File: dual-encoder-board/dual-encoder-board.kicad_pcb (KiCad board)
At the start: 2 copper layers, 27.3 x 27.3 mm, 8 parts, among them U1 EC11EBB24C03

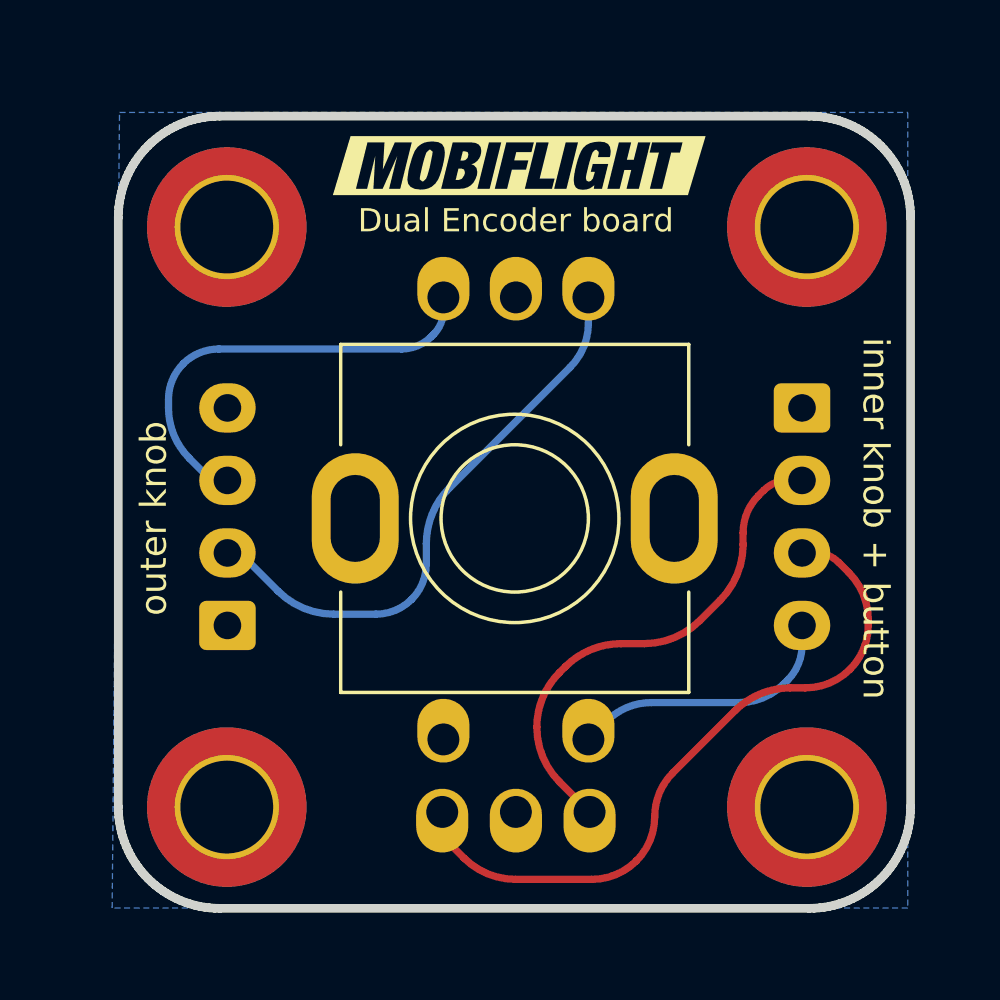
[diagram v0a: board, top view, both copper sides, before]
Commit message: Updates to pcb:   - centered the board outline to mounting holes, was slightly off   - moved the pin labels farther from JST's to avoid DRC errors   - change the unconnected pin 4 of outer knob to just "X" instead of "XX"
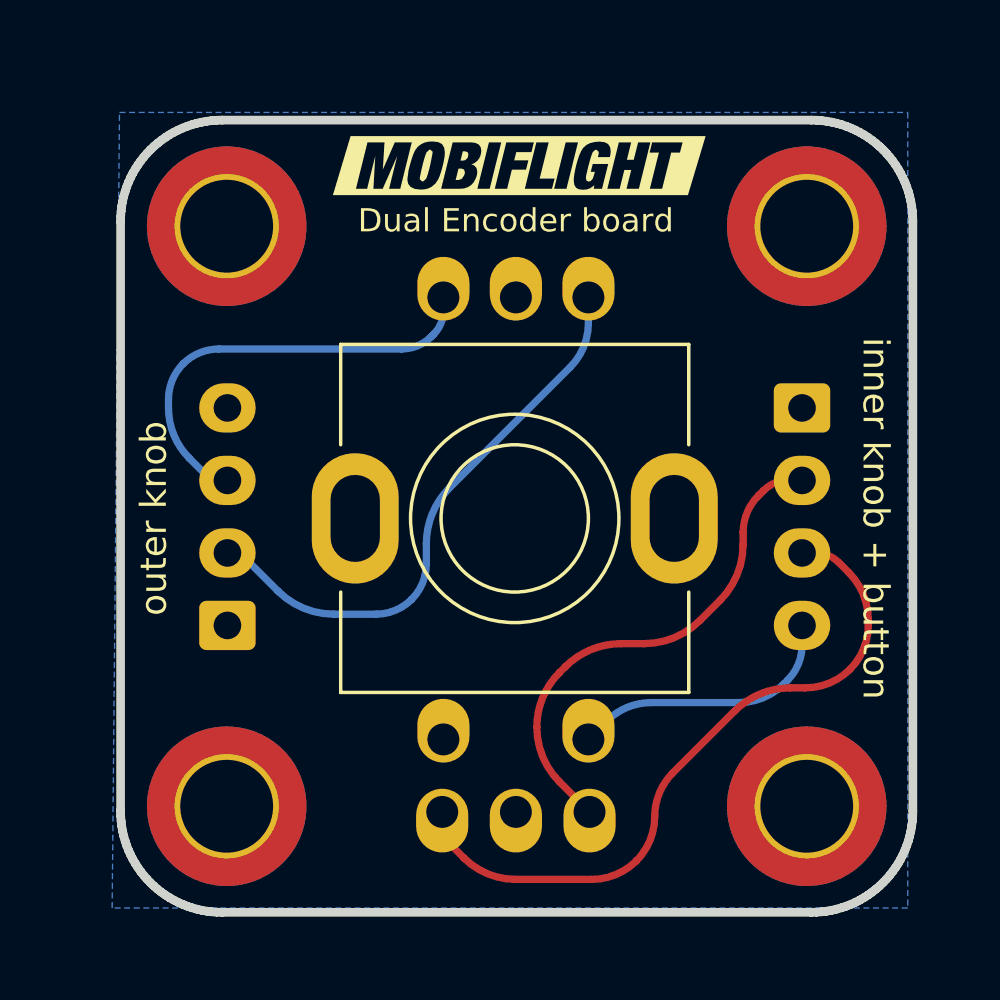
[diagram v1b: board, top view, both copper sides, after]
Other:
- board text added: "G B A X"
- board text removed: "G B A XX"

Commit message: updated button pin to outer encoder connector so it works for single encoders also
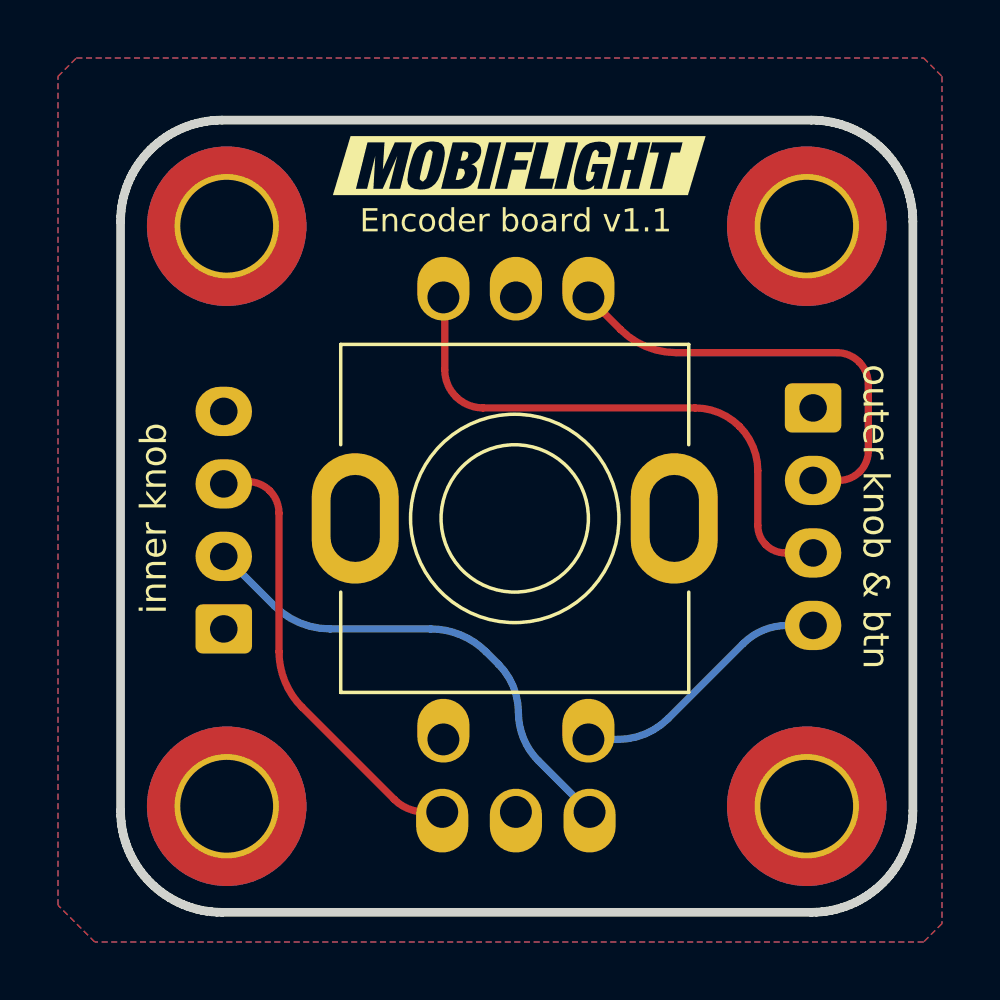
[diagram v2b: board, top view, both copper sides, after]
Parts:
- moved LARGE1 21.5 mm to (128.3, 62.3), turned to -90 degrees
- moved SMALL1 21.3 mm to (108.0, 69.9), turned to 90 degrees
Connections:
- LARGE1 pad 4: unconnected-(LARGE1-Pin_4-Pad4) -> SMALL_BUTTON
- SMALL1 pad 4: SMALL_BUTTON -> unconnected-(SMALL1-Pin_4-Pad4)
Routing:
- net SMALL_B: track 24.3 -> 15.7 mm
- net LARGE_B: track 15.4 -> 19.6 mm
- net LARGE_A: track 19.8 -> 15.7 mm
- net SMALL_A: track 17.5 -> 16.9 mm
- added copper zone on F.Cu, net GND
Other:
- board text added: "20mm"
- board text added: "Encoder board v1.1"
- board text added: "G B A x"
- board text added: "inner knob"
- board text added: "outer knob & btn"
- board text removed: "Dual Encoder board"
- board text removed: "G B A X"
- board text removed: "inner knob + button"
- board text removed: "outer knob"

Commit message: fixed net names
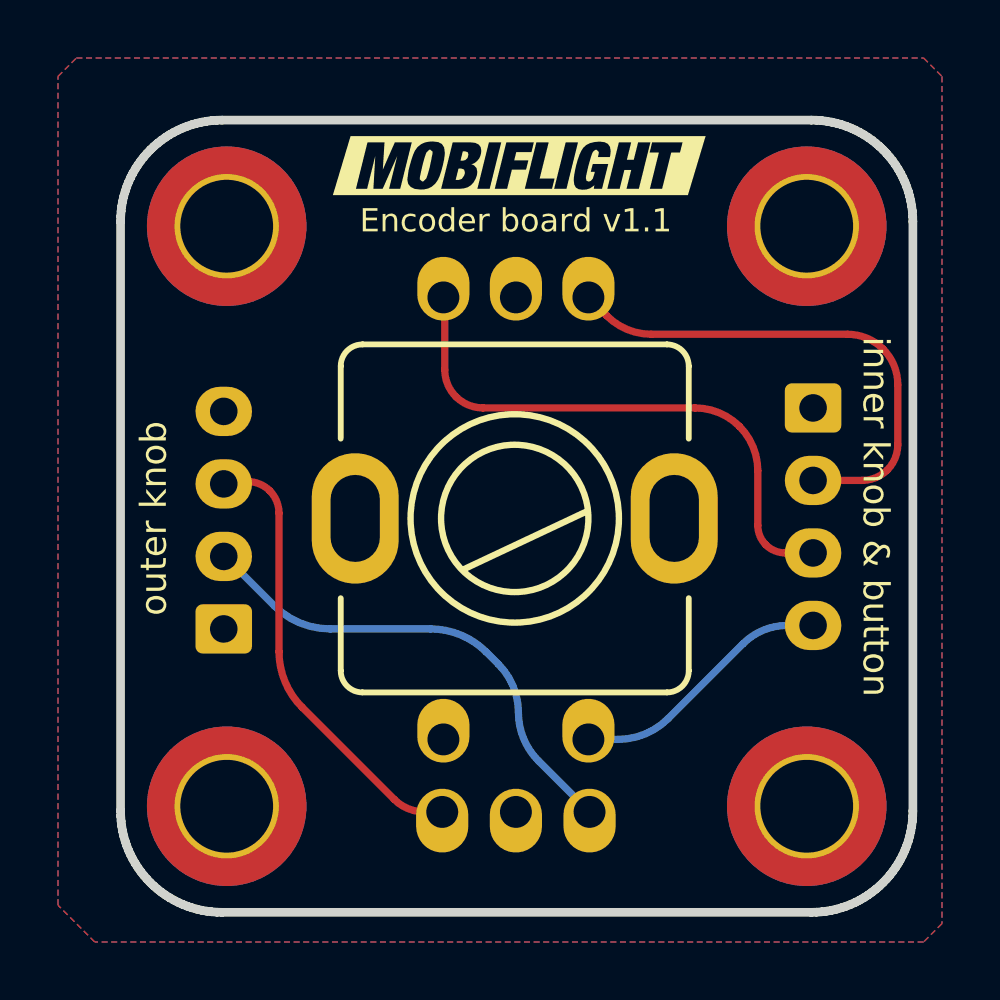
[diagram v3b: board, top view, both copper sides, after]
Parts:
- U1: footprint KiCad:EC11EBB24C03 -> MobiFlight:EC11EBB24C03
- renumbered SMALL1 to LARGE1, LARGE1 to SMALL1
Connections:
- LARGE1 pad 2: SMALL_A -> LARGE_A
- LARGE1 pad 3: SMALL_B -> LARGE_B
- SMALL1 pad 2: LARGE_A -> SMALL_A
- SMALL1 pad 3: LARGE_B -> SMALL_B
- U1 pad A1: LARGE_A -> SMALL_A
- U1 pad A2: SMALL_A -> LARGE_A
- U1 pad B1: LARGE_B -> SMALL_B
- U1 pad B2: SMALL_B -> LARGE_B
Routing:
- net SMALL_B: track 15.7 -> 19.6 mm
- net LARGE_B: track 19.6 -> 15.7 mm
- net LARGE_A: track 15.7 -> 16.9 mm
- net SMALL_A: track 16.9 -> 17.7 mm
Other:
- board text added: "inner knob & button"
- board text added: "outer knob"
- board text removed: "inner knob"
- board text removed: "outer knob & btn"

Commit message: routed the inner a and b traces inside the ground pads (#12)
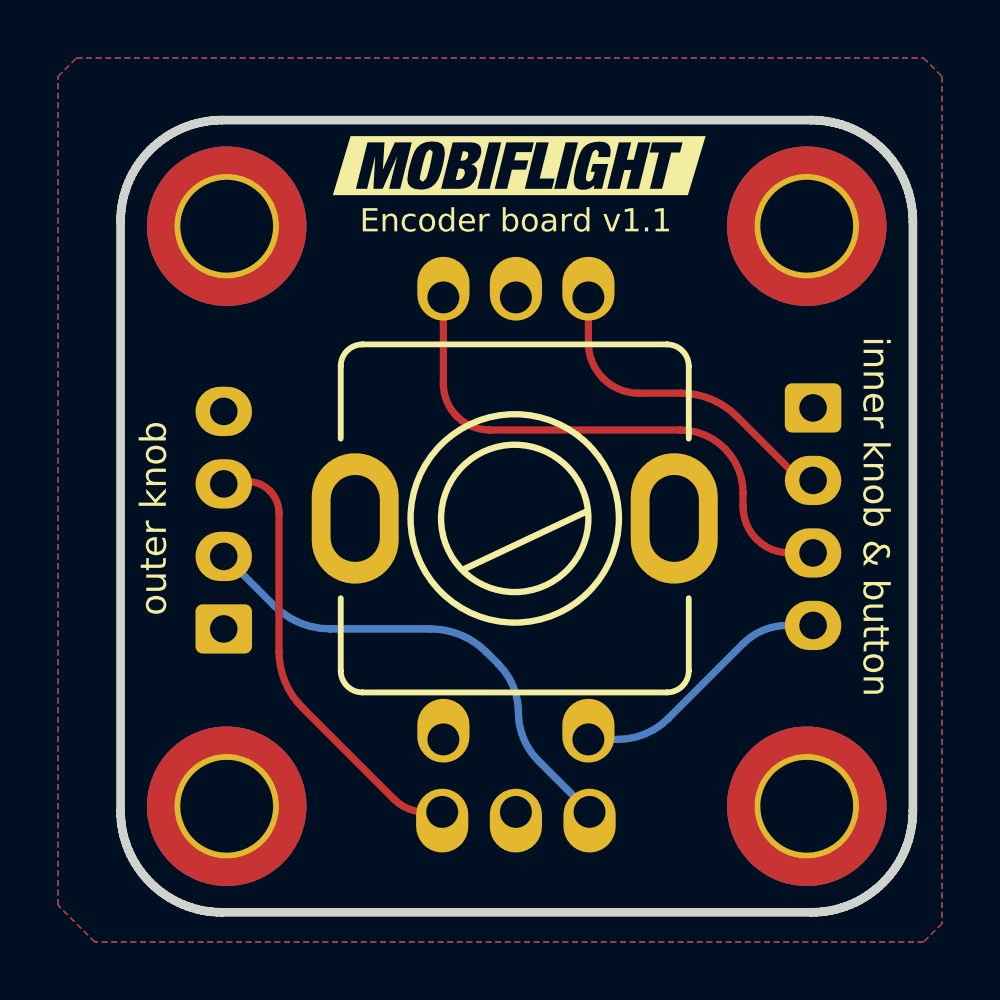
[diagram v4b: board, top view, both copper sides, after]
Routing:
- net SMALL_A: track 17.7 -> 11.4 mm
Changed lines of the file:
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@@
     (effects (font (size 0.8 0.8) (thickness 0.2)))
   )
-  (segment (start 129.468493 59.720016) (end 122.702939 59.720016) (width 0.25) (layer "F.Cu") (net 2))
-  (segment (start 121.169914 59.085016) (end 120.534914 58.450016) (width 0.25) (layer "F.Cu") (net 2))
-  (segment (start 129.970382 64.760016) (end 128.281914 64.760016) (width 0.25) (layer "F.Cu") (net 2))
-  (segment (start 131.202914 63.527484) (end 131.202914 61.454436) (width 0.25) (layer "F.Cu") (net 2))
-  (arc (start 130.841914 64.399016) (mid 130.442051 64.666195) (end 129.970382 64.760016) (width 0.25) (layer "F.Cu") (net 2))
-  (arc (start 130.694914 60.228016) (mid 131.070889 60.790702) (end 131.202914 61.454436) (width 0.25) (layer "F.Cu") (net 2))
-  (arc (start 130.694914 60.228016) (mid 130.132227 59.85204) (end 129.468493 59.720016) (width 0.25) (layer "F.Cu") (net 2))
-  (arc (start 131.202914 63.527484) (mid 131.109093 63.999153) (end 130.841914 64.399016) (width 0.25) (layer "F.Cu") (net 2))
-  (arc (start 121.169914 59.085016) (mid 121.873271 59.554984) (end 122.702939 59.720016) (width 0.25) (layer "F.Cu") (net 2))
-  (segment (start 124.208888 62.260016) (end 116.899902 62.260016) (width 0.25) (layer "F.Cu") (net 3))
-  (segment (start 115.581914 60.942027) (end 115.581914 58.473516) (width 0.25) (layer "F.Cu") (net 3))
-  (segment (start 115.558414 58.450016) (end 115.534914 58.450016) (width 0.25) (layer "F.Cu") (net 3))
-  (segment (start 127.324358 67.260016) (end 128.281914 67.260016) (width 0.25) (layer "F.Cu") (net 3))
-  (segment (start 126.376914 66.312571) (end 126.376914 64.428041) (width 0.25) (layer "F.Cu") (net 3))
-  (arc (start 115.581914 60.942027) (mid 115.682239 61.446399) (end 115.967944 61.873986) (width 0.25) (layer "F.Cu") (net 3))
-  (arc (start 125.741914 62.895016) (mid 125.038555 62.425047) (end 124.208888 62.260016) (width 0.25) (layer "F.Cu") (net 3))
-  (arc (start 115.581914 58.473516) (mid 115.575031 58.456898) (end 115.558414 58.450016) (width 0.25) (layer "F.Cu") (net 3))
-  (arc (start 125.741914 62.895016) (mid 126.211882 63.598373) (end 126.376914 64.428041) (width 0.25) (layer "F.Cu") (net 3))
-  (arc (start 126.376914 66.312571) (mid 126.449033 66.675142) (end 126.654414 66.982516) (width 0.25) (layer "F.Cu") (net 3))
-  (arc (start 126.654414 66.982516) (mid 126.961786 67.187896) (end 127.324358 67.260016) (width 0.25) (layer "F.Cu") (net 3))
-  (arc (start 115.967944 61.873986) (mid 116.39553 62.15969) (end 116.899902 62.260016) (width 0.25) (layer "F.Cu") (net 3))
+  (segment (start 127.712068 64.61117) (end 125.64981 62.548912) (width 0.25) (layer "F.Cu") (net 2))
+  (segment (start 128.071414 64.760016) (end 128.281914 64.760016) (width 0.25) (layer "F.Cu") (net 2))
+  (segment (start 123.725932 61.752016) (end 122.269334 61.752016) (width 0.25) (layer "F.Cu") (net 2))
+  (segment (start 120.534914 60.017595) (end 120.534914 58.450016) (width 0.25) (layer "F.Cu") (net 2))
+  (arc (start 121.042914 61.244016) (mid 121.6056 61.619991) (end 122.269334 61.752016) (width 0.25) (layer "F.Cu") (net 2))
+  (arc (start 125.64981 62.548912) (mid 124.767127 61.959122) (end 123.725932 61.752016) (width 0.25) (layer "F.Cu") (net 2))
+  (arc (start 120.534914 60.017595) (mid 120.666938 60.681329) (end 121.042914 61.244016) (width 0.25) (layer "F.Cu") (net 2))
+  (arc (start 127.712068 64.61117) (mid 127.876937 64.721332) (end 128.071414 64.760016) (width 0.25) (layer "F.Cu") (net 2))
+  (segment (start 115.534914 61.424164) (end 115.534914 58.450016) (width 0.25) (layer "F.Cu") (net 3))
+  (segment (start 127.466765 67.260016) (end 128.281914 67.260016) (width 0.25) (layer "F.Cu") (net 3))
+  (segment (start 117.132765 63.022016) (end 123.700888 63.022016) (width 0.25) (layer "F.Cu") (net 3))
+  (segment (start 125.868914 65.190041) (end 125.868914 65.662164) (width 0.25) (layer "F.Cu") (net 3))
+  (arc (start 115.534914 61.424164) (mid 115.656543 62.035635) (end 116.002914 62.554016) (width 0.25) (layer "F.Cu") (net 3))
+  (arc (start 125.233914 63.657016) (mid 124.530555 63.187047) (end 123.700888 63.022016) (width 0.25) (layer "F.Cu") (net 3))
+  (arc (start 126.336914 66.792016) (mid 126.855294 67.138386) (end 127.466765 67.260016) (width 0.25) (layer "F.Cu") (net 3))
+  (arc (start 125.233914 63.657016) (mid 125.703882 64.360373) (end 125.868914 65.190041) (width 0.25) (layer "F.Cu") (net 3))
+  (arc (start 125.868914 65.662164) (mid 125.990543 66.273635) (end 126.336914 66.792016) (width 0.25) (layer "F.Cu") (net 3))
+  (arc (start 116.002914 62.554016) (mid 116.521294 62.900386) (end 117.132765 63.022016) (width 0.25) (layer "F.Cu") (net 3))
   (segment (start 123.285334 72.971595) (end 125.865821 70.391108) (width 0.25) (layer "B.Cu") (net 4))
   (segment (start 127.389414 69.760016) (end 128.281914 69.760016) (width 0.25) (layer "B.Cu") (net 4))
@@
   (segment (start 108.782901 64.800016) (end 108.001914 64.800016) (width 0.25) (layer "F.Cu") (net 6))
   (segment (start 109.866914 70.658034) (end 109.866914 65.884028) (width 0.25) (layer "F.Cu") (net 6))
-  (arc (start 109.549414 65.117516) (mid 109.784398 65.469194) (end 109.866914 65.884028) (width 0.25) (layer "F.Cu") (net 6))
-  (arc (start 109.549414 65.117516) (mid 109.197734 64.882531) (end 108.782901 64.800016) (width 0.25) (layer "F.Cu") (net 6))
+  (arc (start 109.866914 65.884028) (mid 109.784398 65.469194) (end 109.549414 65.117516) (width 0.25) (layer "F.Cu") (net 6))
+  (arc (start 108.782901 64.800016) (mid 109.197734 64.882531) (end 109.549414 65.117516) (width 0.25) (layer "F.Cu") (net 6))
   (arc (start 113.839518 75.75762) (mid 114.318461 76.077639) (end 114.883414 76.190016) (width 0.25) (layer "F.Cu") (net 6))
-  (arc (start 108.001914 64.800016) (mid 107.973629 64.811731) (end 107.961914 64.840016) (width 0.25) (layer "F.Cu") (net 6))
-  (arc (start 109.866914 70.658034) (mid 110.07402 71.699229) (end 110.66381 72.581912) (width 0.25) (layer "F.Cu") (net 6))
-  (segment (start 117.431777 71.094879) (end 117.01381 70.676912) (width 0.25) (layer "B.Cu") (net 7))
-  (segment (start 115.089932 69.880016) (end 111.628895 69.880016) (width 0.25) (layer "B.Cu") (net 7))
-  (segment (start 109.705017 69.083119) (end 108.016056 67.394158) (width 0.25) (layer "B.Cu") (net 7))
+  (arc (start 107.961914 64.840016) (mid 107.973629 64.811731) (end 108.001914 64.800016) (width 0.25) (layer "F.Cu") (net 6))
+  (arc (start 110.66381 72.581912) (mid 110.07402 71.699229) (end 109.866914 70.658034) (width 0.25) (layer "F.Cu") (net 6))
+  (segment (start 117.01381 70.676912) (end 117.431777 71.094879) (width 0.25) (layer "B.Cu") (net 7))
+  (segment (start 111.628895 69.880016) (end 115.089932 69.880016) (width 0.25) (layer "B.Cu") (net 7))
+  (segment (start 108.016056 67.394158) (end 109.705017 69.083119) (width 0.25) (layer "B.Cu") (net 7))
   (segment (start 118.81205 74.427152) (end 120.574914 76.190016) (width 0.25) (layer "B.Cu") (net 7))
   (segment (start 107.981914 67.380016) (end 107.961914 67.380016) (width 0.25) (layer "B.Cu") (net 7))
-  (arc (start 117.431777 71.094879) (mid 117.942553 71.859309) (end 118.121914 72.761016) (width 0.25) (layer "B.Cu") (net 7))
-  (arc (start 118.121914 72.761016) (mid 118.301274 73.662722) (end 118.81205 74.427152) (width 0.25) (layer "B.Cu") (net 7))
-  (arc (start 108.016056 67.394158) (mid 108.000391 67.383691) (end 107.981914 67.380016) (width 0.25) (layer "B.Cu") (net 7))
+  (arc (start 118.121914 72.761016) (mid 117.942553 71.859309) (end 117.431777 71.094879) (width 0.25) (layer "B.Cu") (net 7))
+  (arc (start 118.81205 74.427152) (mid 118.301274 73.662722) (end 118.121914 72.761016) (width 0.25) (layer "B.Cu") (net 7))
+  (arc (start 107.981914 67.380016) (mid 108.000391 67.383691) (end 108.016056 67.394158) (width 0.25) (layer "B.Cu") (net 7))
   (arc (start 109.705017 69.083119) (mid 110.5877 69.672909) (end 111.628895 69.880016) (width 0.25) (layer "B.Cu") (net 7))
   (arc (start 117.01381 70.676912) (mid 116.131127 70.087122) (end 115.089932 69.880016) (width 0.25) (layer "B.Cu") (net 7))

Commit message: Updated labels to perfection :-) (#13)
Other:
- board text added: "CONNECTOR SIDE"
- board text added: "ENCODER SIDE"
- board text added: "Encoder board"
- board text added: "v1.1"
- board text removed: "Encoder board v1.1"
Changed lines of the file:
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@@
     (effects (font (size 1 1) (thickness 0.2)) (justify mirror))
+  )
+  (gr_text "v1.1" (at 117.994914 53.878016) (layer "B.SilkS")
+    (effects (font (size 0.8 0.8) (thickness 0.2)) (justify mirror))
+  )
+  (gr_text "CONNECTOR\nSIDE" (at 117.994914 70.134016) (layer "B.SilkS")
+    (effects (font (size 0.8 0.8) (thickness 0.2)) (justify mirror))
   )
   (gr_text "inner knob & button\n" (at 130.440914 66.010016 270) (layer "F.SilkS")
@@
     (effects (font (size 0.9 0.9) (thickness 0.2)))
   )
-  (gr_text "Encoder board v1.1" (at 118.030102 55.802118) (layer "F.SilkS")
+  (gr_text "ENCODER SIDE" (at 117.994914 70.896016) (layer "F.SilkS")
     (effects (font (size 0.8 0.8) (thickness 0.2)))
   )
+  (gr_text "Encoder board\n" (at 117.994914 55.910016) (layer "F.SilkS")
+    (effects (font (size 0.8 0.8) (thickness 0.2)))
+  )
